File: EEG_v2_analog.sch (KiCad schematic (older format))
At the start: 53 parts, among them U1 ADS1299IPAGR

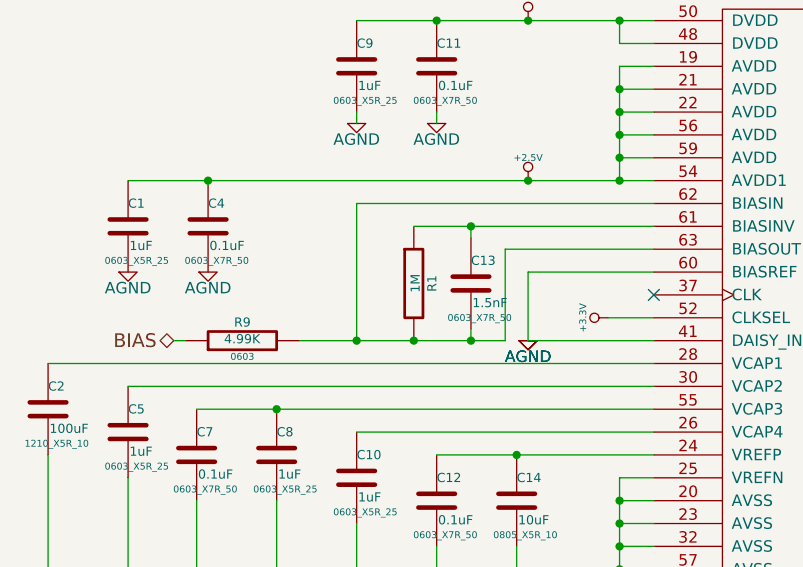
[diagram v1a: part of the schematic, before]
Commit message: Add footprints
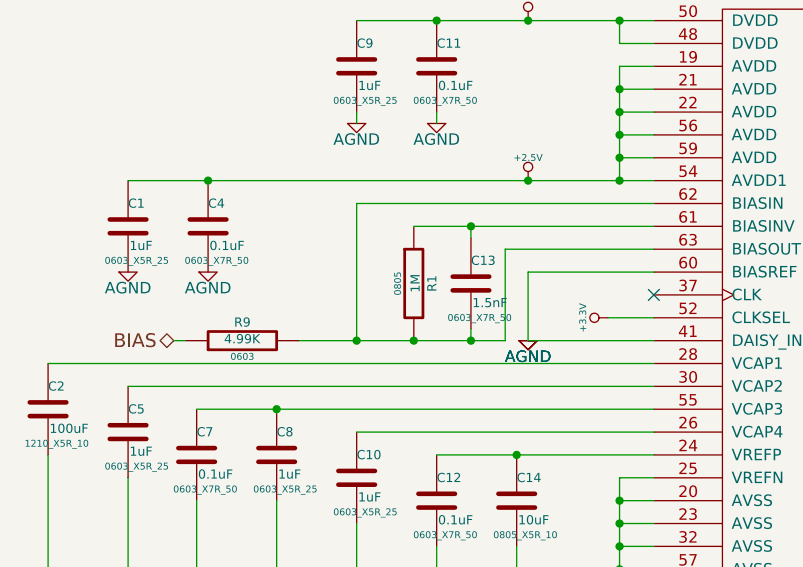
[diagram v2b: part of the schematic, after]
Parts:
- R1: footprint ~ -> 0805
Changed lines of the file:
@@
 $EndComp
 $Comp
-L +3.3V #PWR04
+L +3.3V #PWR06
 U 1 1 54B45DA4
 P 2750 2750
-F 0 "#PWR04" H 2750 2710 30  0001 C CNN
+F 0 "#PWR06" H 2750 2710 30  0001 C CNN
 F 1 "+3.3V" H 2750 2860 30  0000 C CNN
 F 2 "" H 2750 2750 60  0000 C CNN
@@
 $EndComp
 $Comp
-L +2.5V #PWR05
+L +2.5V #PWR07
 U 1 1 54B45DB6
 P 2750 3450
-F 0 "#PWR05" H 2750 3400 20  0001 C CNN
+F 0 "#PWR07" H 2750 3400 20  0001 C CNN
 F 1 "+2.5V" H 2750 3550 30  0000 C CNN
 F 2 "" H 2750 3450 60  0000 C CNN
@@
 $EndComp
 $Comp
-L AGND #PWR06
+L AGND #PWR08
 U 1 1 54B45DC8
 P 1000 3850
-F 0 "#PWR06" H 1000 3850 40  0001 C CNN
+F 0 "#PWR08" H 1000 3850 40  0001 C CNN
 F 1 "AGND" H 1000 3780 50  0000 C CNN
 F 2 "" H 1000 3850 60  0000 C CNN
@@
 $EndComp
 $Comp
-L AGND #PWR07
+L AGND #PWR09
 U 1 1 54B45DCE
 P 1350 3850
-F 0 "#PWR07" H 1350 3850 40  0001 C CNN
+F 0 "#PWR09" H 1350 3850 40  0001 C CNN
 F 1 "AGND" H 1350 3780 50  0000 C CNN
 F 2 "" H 1350 3850 60  0000 C CNN
@@
 $EndComp
 $Comp
-L AGND #PWR08
+L AGND #PWR010
 U 1 1 54B45E0A
 P 900 5900
-F 0 "#PWR08" H 900 5900 40  0001 C CNN
+F 0 "#PWR010" H 900 5900 40  0001 C CNN
 F 1 "AGND" H 900 5830 50  0000 C CNN
 F 2 "" H 900 5900 60  0000 C CNN
@@
 $EndComp
 $Comp
-L -2.5V #PWR09
+L -2.5V #PWR011
 U 1 1 54B45E16
 P 2350 5350
-F 0 "#PWR09" H 2350 5300 20  0001 C CNN
+F 0 "#PWR011" H 2350 5300 20  0001 C CNN
 F 1 "-2.5V" H 2350 5450 30  0000 C CNN
 F 2 "" H 2350 5350 60  0000 C CNN
@@
 $EndComp
 $Comp
-L +3.3V #PWR010
+L +3.3V #PWR012
 U 1 1 54B45E1C
 P 3100 4050
-F 0 "#PWR010" H 3100 4010 30  0001 C CNN
+F 0 "#PWR012" H 3100 4010 30  0001 C CNN
 F 1 "+3.3V" H 3100 4160 30  0000 C CNN
 F 2 "" H 3100 4050 60  0000 C CNN
@@
 NoConn ~ 3300 3950
 $Comp
-L +3.3V #PWR011
+L +3.3V #PWR013
 U 1 1 54B45E23
 P 5850 2950
-F 0 "#PWR011" H 5850 2910 30  0001 C CNN
+F 0 "#PWR013" H 5850 2910 30  0001 C CNN
 F 1 "+3.3V" H 5850 3060 30  0000 C CNN
 F 2 "" H 5850 2950 60  0000 C CNN
@@
 F 0 "R1" V 2330 3900 40  0000 C CNN
 F 1 "1M" V 2257 3901 40  0000 C CNN
-F 2 "~" V 2180 3900 30  0000 C CNN
+F 2 "0805" V 2180 3900 30  0000 C CNN
 F 3 "~" H 2250 3900 30  0000 C CNN
 	1    2250 3900
@@
 	3300 5050 3150 5050
 $Comp
-L AGND #PWR012
+L AGND #PWR014
 U 1 1 54B45E8A
 P 2350 3200
-F 0 "#PWR012" H 2350 3200 40  0001 C CNN
+F 0 "#PWR014" H 2350 3200 40  0001 C CNN
 F 1 "AGND" H 2350 3130 50  0000 C CNN
 F 2 "" H 2350 3200 60  0000 C CNN
@@
 $EndComp
 $Comp
-L AGND #PWR013
+L AGND #PWR015
 U 1 1 54B45E90
 P 2000 3200
-F 0 "#PWR013" H 2000 3200 40  0001 C CNN
+F 0 "#PWR015" H 2000 3200 40  0001 C CNN
 F 1 "AGND" H 2000 3130 50  0000 C CNN
 F 2 "" H 2000 3200 60  0000 C CNN
@@
 DRDY
 $Comp
-L AGND #PWR014
+L AGND #PWR016
 U 1 1 54B4B08F
 P 2750 4150
-F 0 "#PWR014" H 2750 4150 40  0001 C CNN
+F 0 "#PWR016" H 2750 4150 40  0001 C CNN
 F 1 "AGND" H 2750 4080 50  0000 C CNN
 F 2 "" H 2750 4150 60  0000 C CNN
@@
 $EndComp
 $Comp
-L AGND #PWR015
+L AGND #PWR017
 U 1 1 54B4B095
 P 2750 4150
-F 0 "#PWR015" H 2750 4150 40  0001 C CNN
+F 0 "#PWR017" H 2750 4150 40  0001 C CNN
 F 1 "AGND" H 2750 4080 50  0000 C CNN
 F 2 "" H 2750 4150 60  0000 C CNN
@@
 Connection ~ 900  5850
 $Comp
-L AGND #PWR016
+L AGND #PWR018
 U 1 1 54C4ED9D
 P 6000 3550
-F 0 "#PWR016" H 6000 3550 40  0001 C CNN
+F 0 "#PWR018" H 6000 3550 40  0001 C CNN
 F 1 "AGND" H 6000 3480 50  0000 C CNN
 F 2 "" H 6000 3550 60  0000 C CNN
@@
 $EndComp
 $Comp
-L -2.5V #PWR017
+L -2.5V #PWR019
 U 1 1 54C4F2A1
 P 1000 1350
-F 0 "#PWR017" H 1000 1300 20  0001 C CNN
+F 0 "#PWR019" H 1000 1300 20  0001 C CNN
 F 1 "-2.5V" H 1000 1450 30  0000 C CNN
 F 2 "" H 1000 1350 60  0000 C CNN
@@
 $EndComp
 $Comp
-L +2.5V #PWR018
+L +2.5V #PWR020
 U 1 1 54C4F2B1
 P 1000 750
-F 0 "#PWR018" H 1000 700 20  0001 C CNN
+F 0 "#PWR020" H 1000 700 20  0001 C CNN
 F 1 "+2.5V" H 1000 850 30  0000 C CNN
 F 2 "" H 1000 750 60  0000 C CNN
@@
 $EndComp
 $Comp
-L AGND #PWR019
+L AGND #PWR021
 U 1 1 54C7F838
 P 6850 1200
-F 0 "#PWR019" H 6850 1200 40  0001 C CNN
+F 0 "#PWR021" H 6850 1200 40  0001 C CNN
 F 1 "AGND" H 6850 1130 50  0000 C CNN
 F 2 "" H 6850 1200 60  0000 C CNN
@@
 	7000 3200 6850 3200
 $Comp
-L AGND #PWR020
+L AGND #PWR022
 U 1 1 54C7FC68
 P 6850 3200
-F 0 "#PWR020" H 6850 3200 40  0001 C CNN
+F 0 "#PWR022" H 6850 3200 40  0001 C CNN
 F 1 "AGND" H 6850 3130 50  0000 C CNN
 F 2 "" H 6850 3200 60  0000 C CNN
@@
 	7000 4200 6850 4200
 $Comp
-L AGND #PWR021
+L AGND #PWR023
 U 1 1 54C7FC8F
 P 6850 4200
-F 0 "#PWR021" H 6850 4200 40  0001 C CNN
+F 0 "#PWR023" H 6850 4200 40  0001 C CNN
 F 1 "AGND" H 6850 4130 50  0000 C CNN
 F 2 "" H 6850 4200 60  0000 C CNN
@@
 	7000 5200 6850 5200
 $Comp
-L AGND #PWR022
+L AGND #PWR024
 U 1 1 54C7FCB6
 P 6850 5200
-F 0 "#PWR022" H 6850 5200 40  0001 C CNN
+F 0 "#PWR024" H 6850 5200 40  0001 C CNN
 F 1 "AGND" H 6850 5130 50  0000 C CNN
 F 2 "" H 6850 5200 60  0000 C CNN
@@
 	7000 6200 6850 6200
 $Comp
-L AGND #PWR023
+L AGND #PWR025
 U 1 1 54C7FCDD
 P 6850 6200
-F 0 "#PWR023" H 6850 6200 40  0001 C CNN
+F 0 "#PWR025" H 6850 6200 40  0001 C CNN
 F 1 "AGND" H 6850 6130 50  0000 C CNN
 F 2 "" H 6850 6200 60  0000 C CNN
@@
 	7000 7200 6850 7200
 $Comp
-L AGND #PWR024
+L AGND #PWR026
 U 1 1 54C7FD04
 P 6850 7200
-F 0 "#PWR024" H 6850 7200 40  0001 C CNN
+F 0 "#PWR026" H 6850 7200 40  0001 C CNN
 F 1 "AGND" H 6850 7130 50  0000 C CNN
 F 2 "" H 6850 7200 60  0000 C CNN
@@
 	7000 8200 6850 8200
 $Comp
-L AGND #PWR025
+L AGND #PWR027
 U 1 1 54C7FD2B
 P 6850 8200
-F 0 "#PWR025" H 6850 8200 40  0001 C CNN
+F 0 "#PWR027" H 6850 8200 40  0001 C CNN
 F 1 "AGND" H 6850 8130 50  0000 C CNN
 F 2 "" H 6850 8200 60  0000 C CNN
@@
 	6050 6550 6050 5550
 $Comp
-L AGND #PWR026
+L AGND #PWR028
 U 1 1 54C824DA
 P 5650 7000
-F 0 "#PWR026" H 5650 7000 40  0001 C CNN
+F 0 "#PWR028" H 5650 7000 40  0001 C CNN
 F 1 "AGND" H 5650 6930 50  0000 C CNN
 F 2 "" H 5650 7000 60  0000 C CNN
@@
 	3150 5450 3150 6000
 $Comp
-L AGND #PWR027
+L AGND #PWR029
 U 1 1 54CC83F7
 P 3150 6000
-F 0 "#PWR027" H 3150 6000 40  0001 C CNN
+F 0 "#PWR029" H 3150 6000 40  0001 C CNN
 F 1 "AGND" H 3150 5930 50  0000 C CNN
 F 2 "" H 3150 6000 60  0000 C CNN
@@
 Connection ~ 3150 5750
 $Comp
-L AGND #PWR028
+L AGND #PWR030
 U 1 1 54CC881D
 P 6850 2200
-F 0 "#PWR028" H 6850 2200 40  0001 C CNN
+F 0 "#PWR030" H 6850 2200 40  0001 C CNN
 F 1 "AGND" H 6850 2130 50  0000 C CNN
 F 2 "" H 6850 2200 60  0000 C CNN

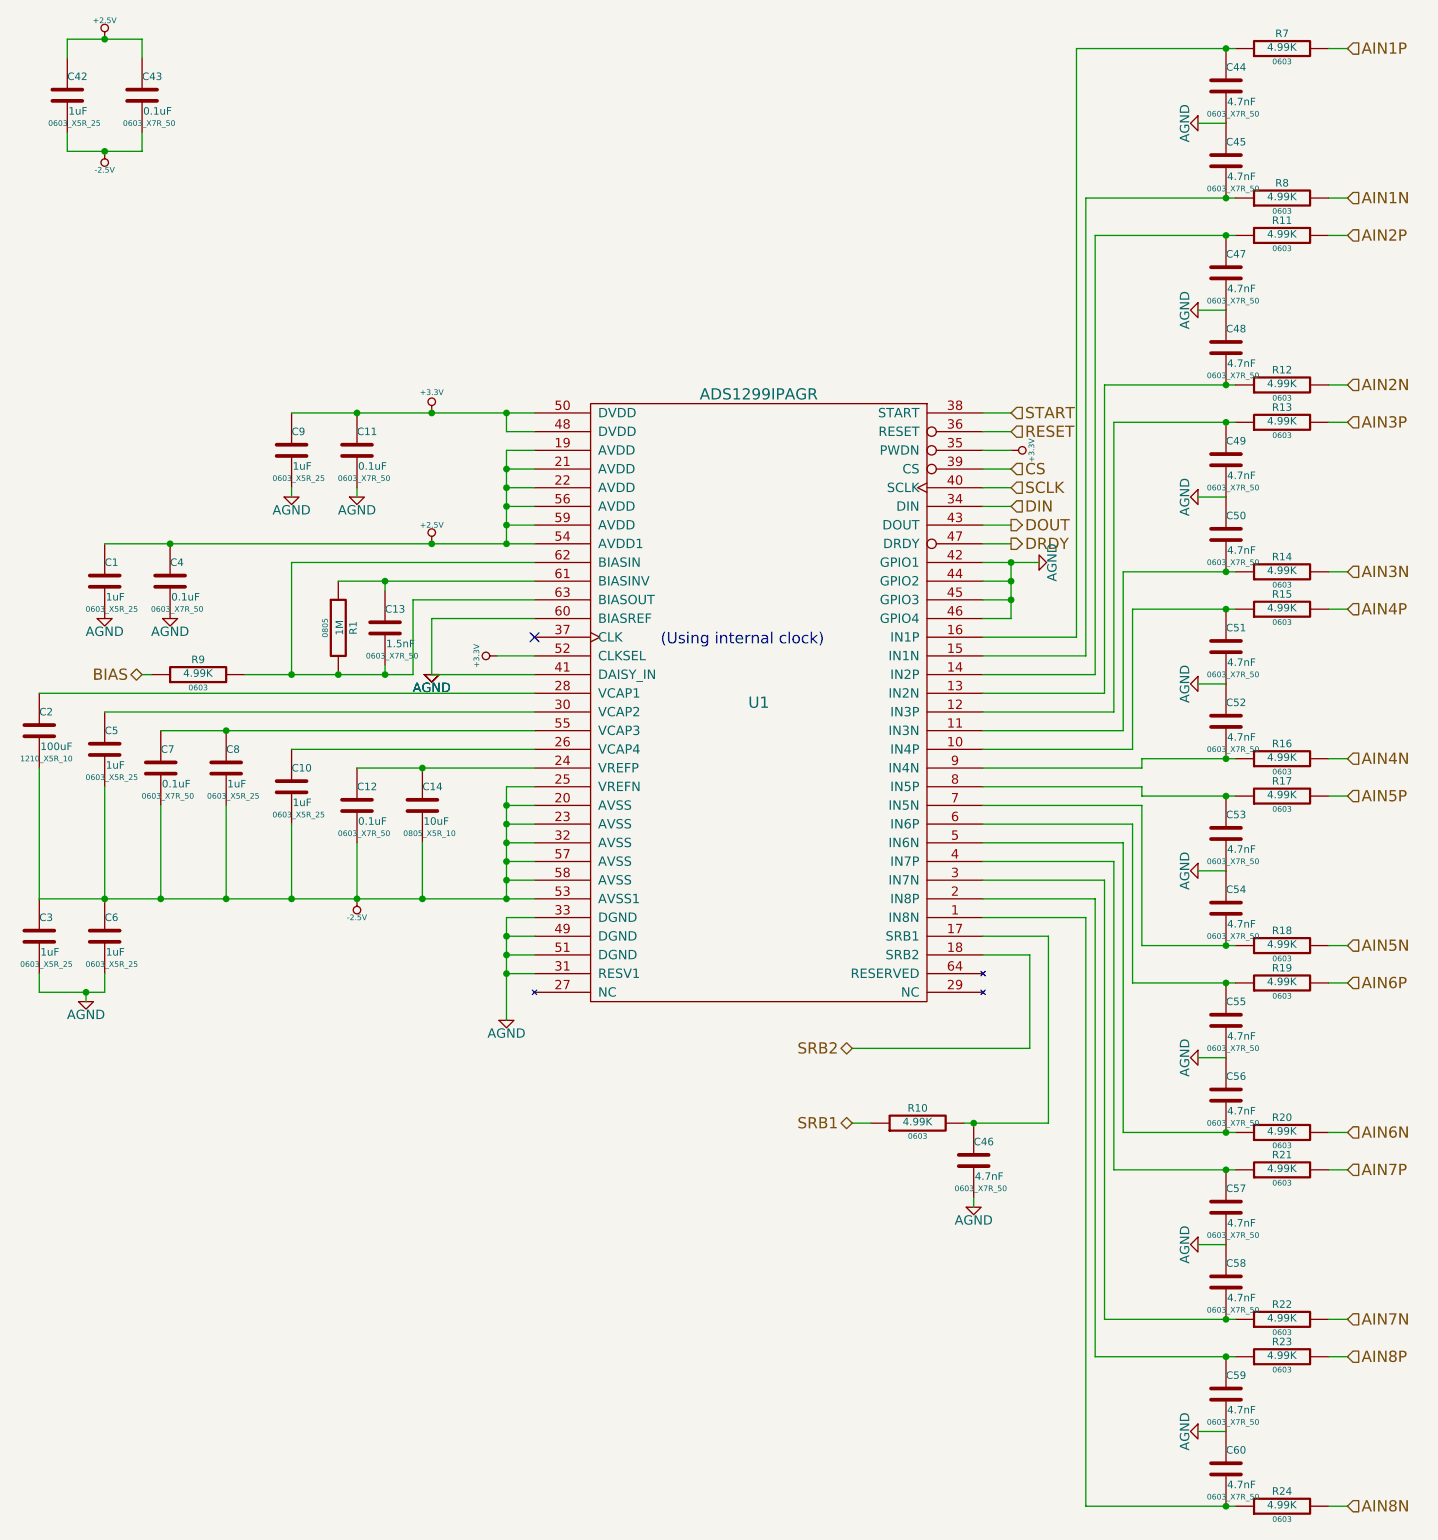
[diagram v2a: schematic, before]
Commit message: Added footprints to connectors. Changed usb A to usb micro B
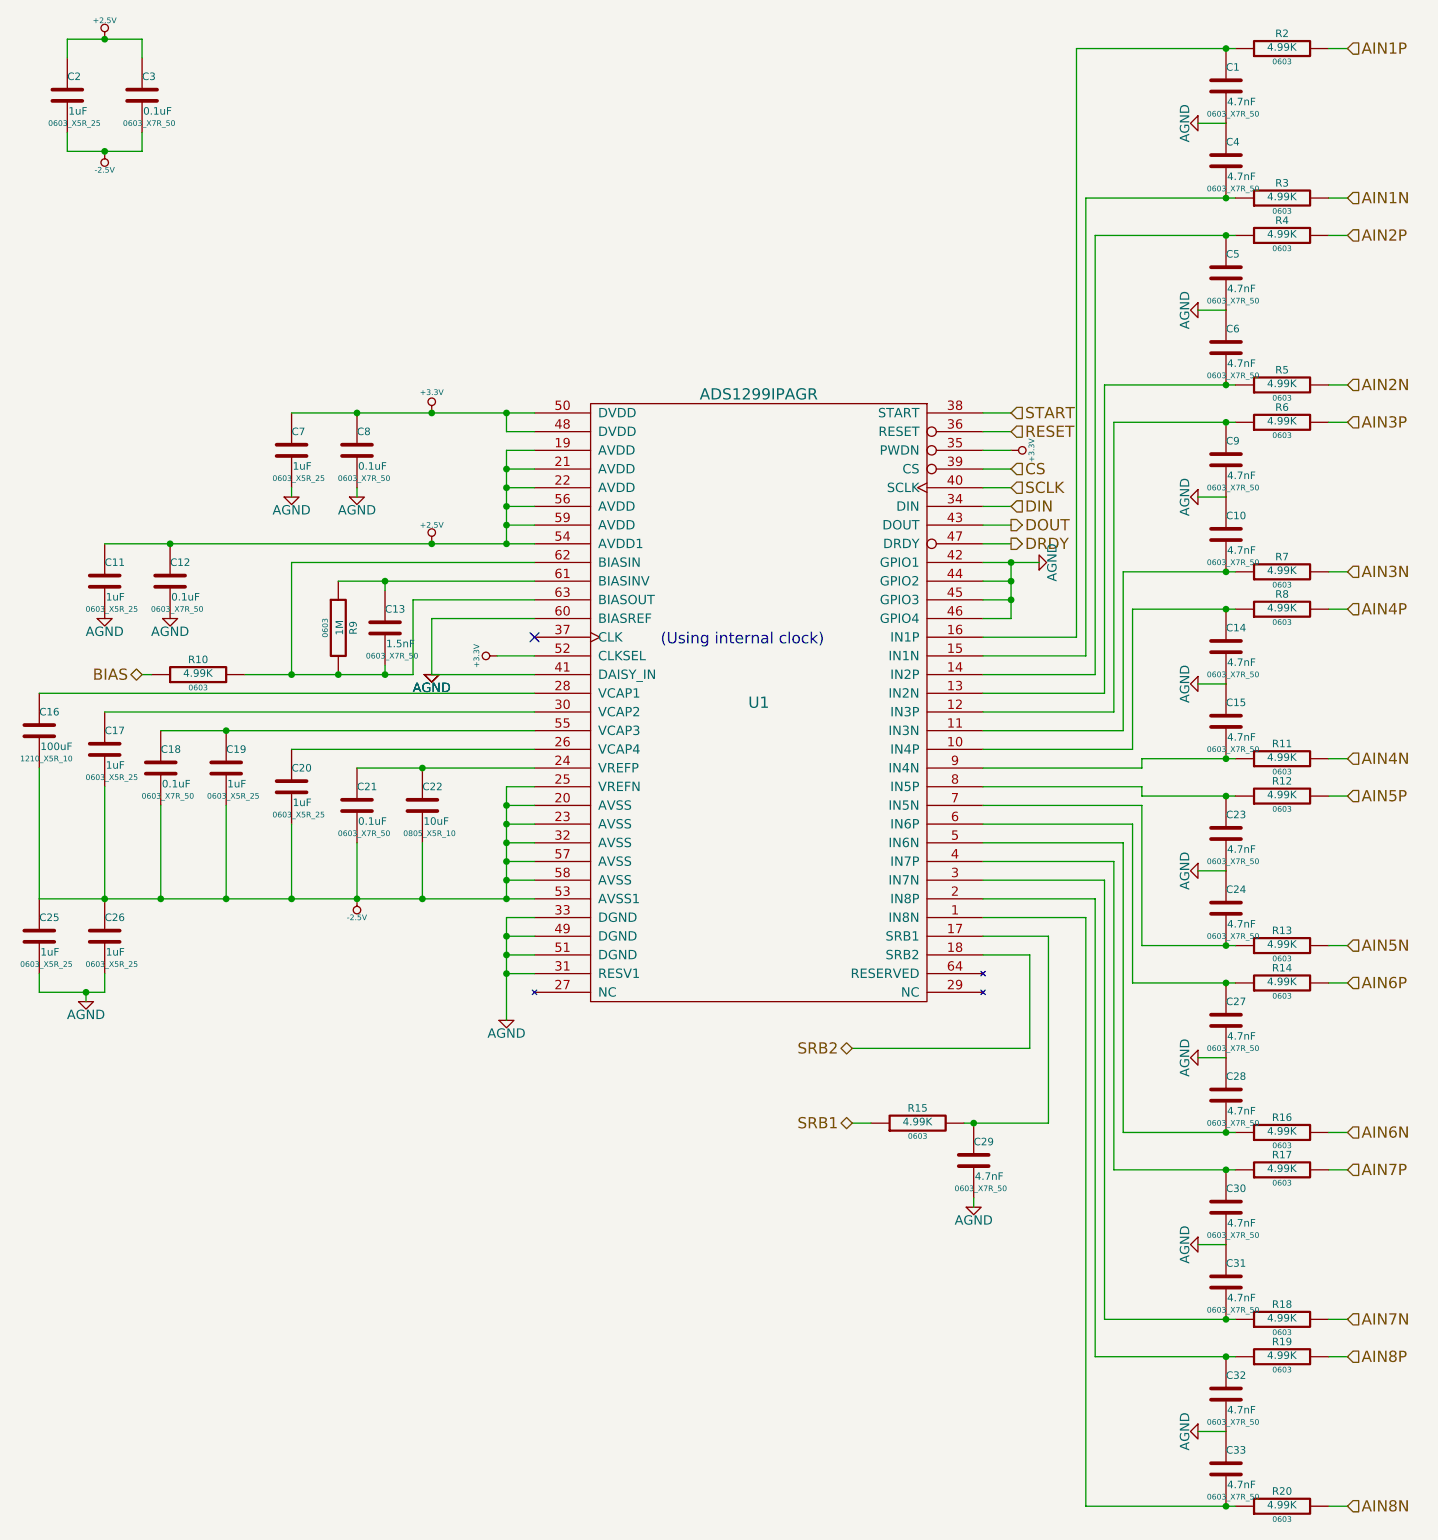
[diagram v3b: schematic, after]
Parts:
- R9: renamed from R1; footprint 0805 -> 0603
- renumbered C44 to C1, C50 to C10, C1 to C11, C4 to C12, C51 to C14, C52 to C15, C2 to C16, C5 to C17, C7 to C18, C8 to C19, C42 to C2, C10 to C20, C12 to C21, C14 to C22, C53 to C23, C54 to C24, C3 to C25, C6 to C26, C55 to C27, C56 to C28, C46 to C29, C43 to C3, C57 to C30, C58 to C31, C59 to C32, C60 to C33, C45 to C4, C47 to C5, C48 to C6, C9 to C7, C11 to C8, C49 to C9, R9 to R10, R16 to R11, R17 to R12, R18 to R13, R19 to R14, R10 to R15, R20 to R16, R21 to R17, R22 to R18, R23 to R19, R7 to R2, R24 to R20, R8 to R3, R11 to R4, R12 to R5, R13 to R6, R14 to R7, R15 to R8

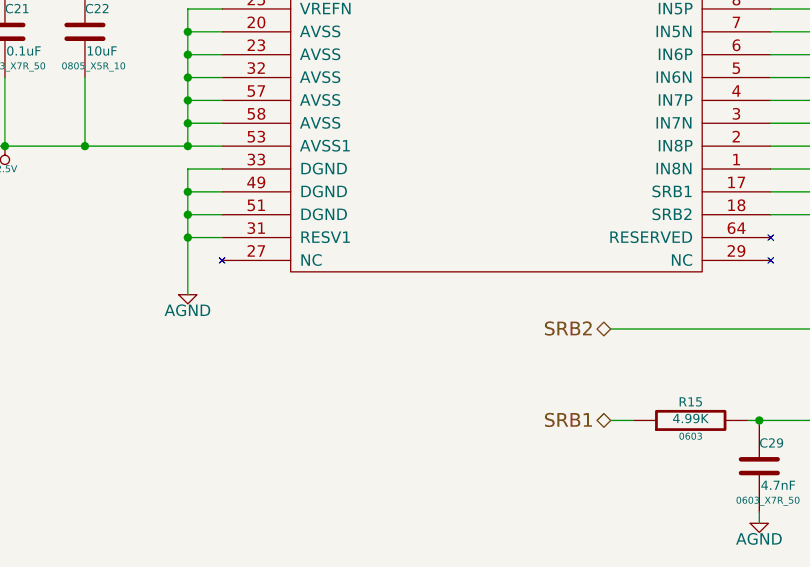
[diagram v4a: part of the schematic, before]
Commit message: Add footprints for tactile switches
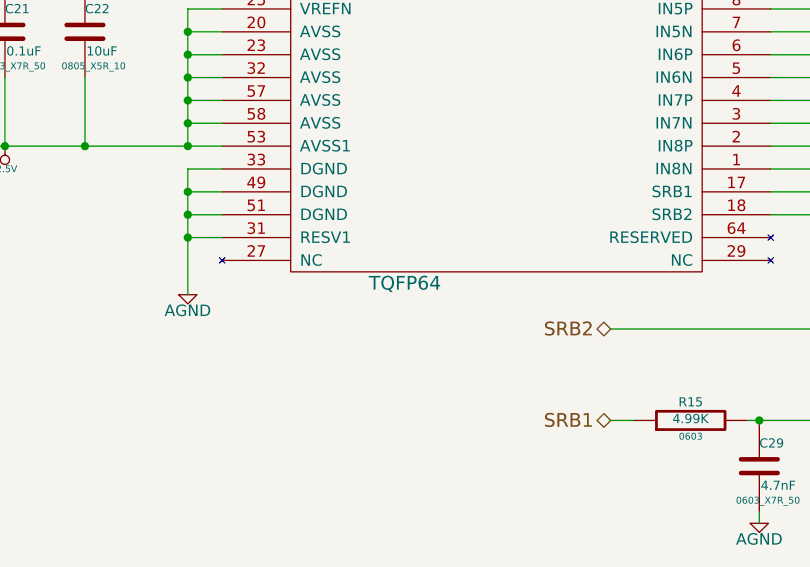
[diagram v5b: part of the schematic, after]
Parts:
- U1: footprint (none) -> TQFP64
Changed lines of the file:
@@
 F 0 "U1" H 4500 4300 60  0000 C CNN
 F 1 "ADS1299IPAGR" H 4500 5950 60  0000 C CNN
-F 2 "" H 4500 5950 60  0000 C CNN
+F 2 "TQFP64" H 4100 2650 60  0000 C CNN
 F 3 "http://www.ti.com/lit/ds/symlink/ads1299.pdf" H 4500 5950 60  0001 C CNN
 	1    4500 4300

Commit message: Associate footprints to pcbnew
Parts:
- C13: footprint 0603_X7R_50 -> 0805
- R9: footprint 0603 -> 0805
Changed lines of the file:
@@
 F 0 "C13" H 2500 4000 40  0000 L CNN
 F 1 "1.5nF" H 2506 3815 40  0000 L CNN
-F 2 "0603_X7R_50" H 2538 3750 30  0000 C CNN
+F 2 "0805" H 2538 3750 30  0000 C CNN
 F 3 "~" H 2500 3900 60  0000 C CNN
 	1    2500 3900
@@
 F 0 "R9" V 2330 3900 40  0000 C CNN
 F 1 "1M" V 2257 3901 40  0000 C CNN
-F 2 "0603" V 2180 3900 30  0000 C CNN
+F 2 "0805" V 2180 3900 30  0000 C CNN
 F 3 "~" H 2250 3900 30  0000 C CNN
 	1    2250 3900

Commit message: Continued layout work.
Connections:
- net AGND: now also C10.2, C15.2, C24.2, C28.2, C31.2, C33.2, C4.2, C6.2; no longer C10.1, C15.1, C24.1, C28.1, C31.1, C33.1, C4.1, C6.1
- net at R20.1, U1.1 (IN8N): now also C33.1; no longer C33.2
- net at R7.1, U1.11 (IN3N): now also C10.1; no longer C10.2
- net at R5.1, U1.13 (IN2N): now also C6.1; no longer C6.2
- net at R3.1, U1.15 (IN1N): now also C4.1; no longer C4.2
- net at R18.1, U1.3 (IN7N): now also C31.1; no longer C31.2
- net at R16.1, U1.5 (IN6N): now also C28.1; no longer C28.2
- net at R13.1, U1.7 (IN5N): now also C24.1; no longer C24.2
- net at R11.1, U1.9 (IN4N): now also C15.1; no longer C15.2
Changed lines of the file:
@@
 F 3 "~" H 7000 1400 60  0000 C CNN
 	1    7000 1400
-	1    0    0    -1
+	-1   0    0    1
 $EndComp
 $Comp
@@
 F 3 "~" H 7000 2400 60  0000 C CNN
 	1    7000 2400
-	1    0    0    -1
+	-1   0    0    1
 $EndComp
 $Comp
@@
 F 3 "~" H 7000 3400 60  0000 C CNN
 	1    7000 3400
-	1    0    0    -1
+	-1   0    0    1
 $EndComp
 Wire Wire Line
@@
 F 3 "~" H 7000 4400 60  0000 C CNN
 	1    7000 4400
-	1    0    0    -1
+	-1   0    0    1
 $EndComp
 Wire Wire Line
@@
 F 3 "~" H 7000 5400 60  0000 C CNN
 	1    7000 5400
-	1    0    0    -1
+	-1   0    0    1
 $EndComp
 Wire Wire Line
@@
 F 3 "~" H 7000 6400 60  0000 C CNN
 	1    7000 6400
-	1    0    0    -1
+	-1   0    0    1
 $EndComp
 Wire Wire Line
@@
 F 3 "~" H 7000 7400 60  0000 C CNN
 	1    7000 7400
-	1    0    0    -1
+	-1   0    0    1
 $EndComp
 Wire Wire Line
@@
 F 3 "~" H 7000 8400 60  0000 C CNN
 	1    7000 8400
-	1    0    0    -1
-$EndComp
-Wire Wire Line
+	-1   0    0    1
+$EndComp
+Wire Wire Line
